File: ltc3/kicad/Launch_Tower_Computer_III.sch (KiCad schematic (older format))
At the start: 0 parts

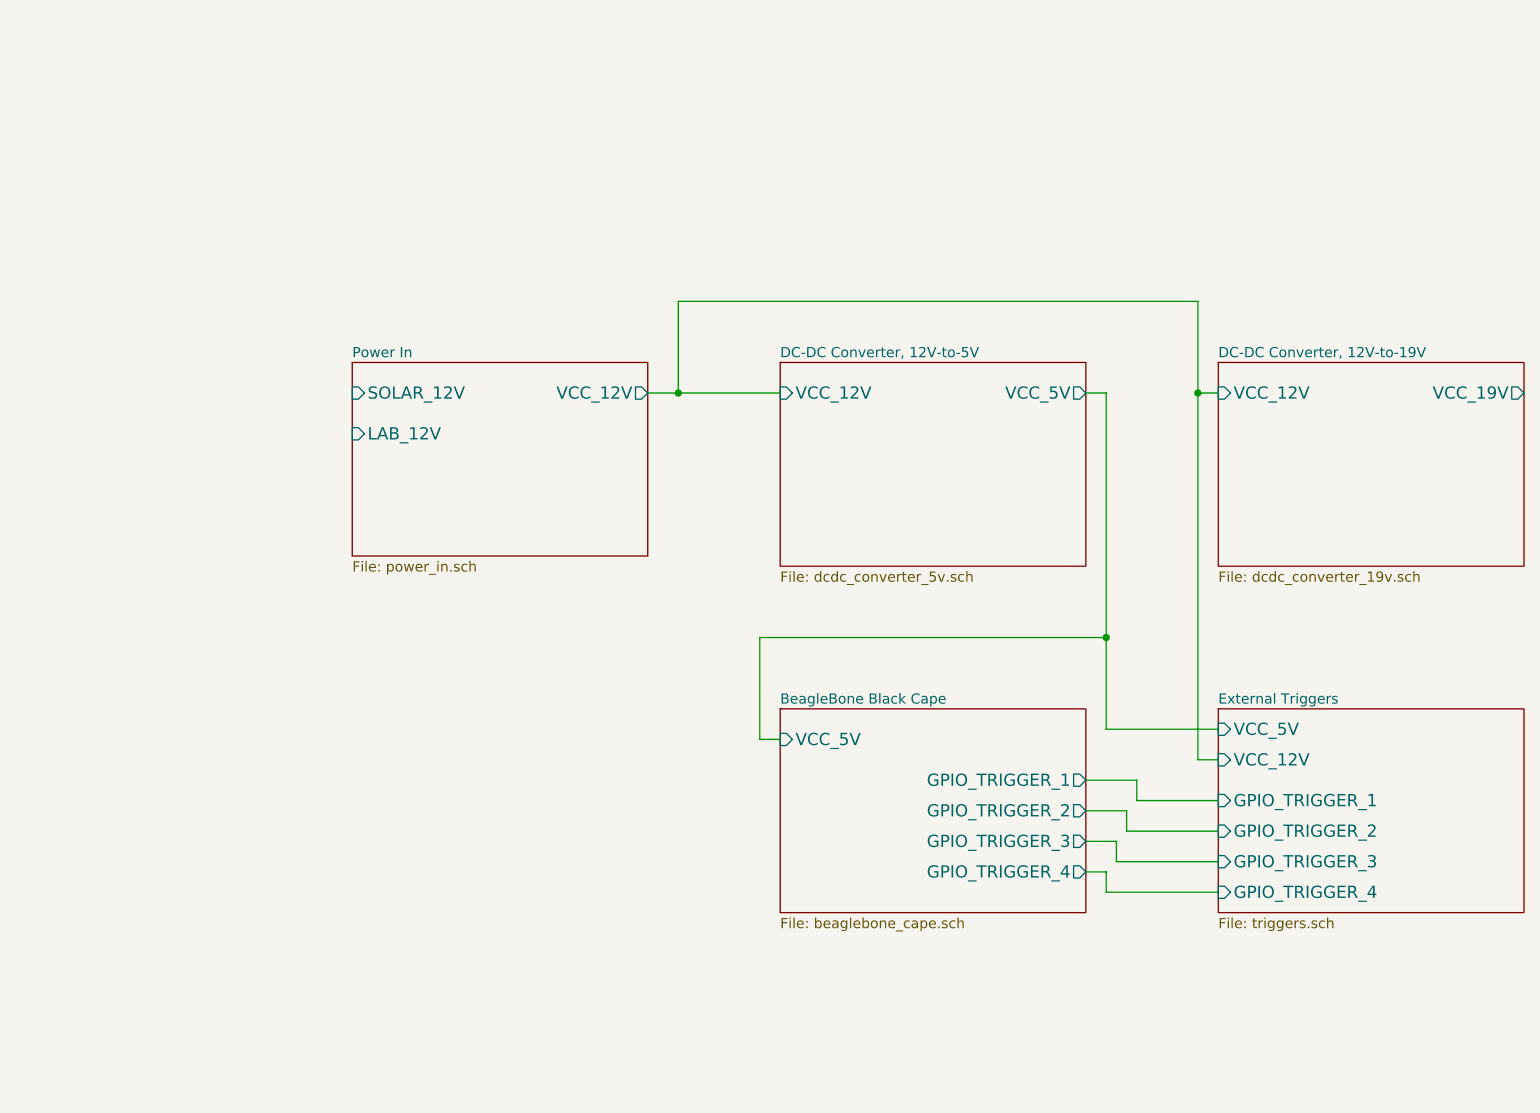
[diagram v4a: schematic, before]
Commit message: Incremental progress on LTC3 design spec, schematic.
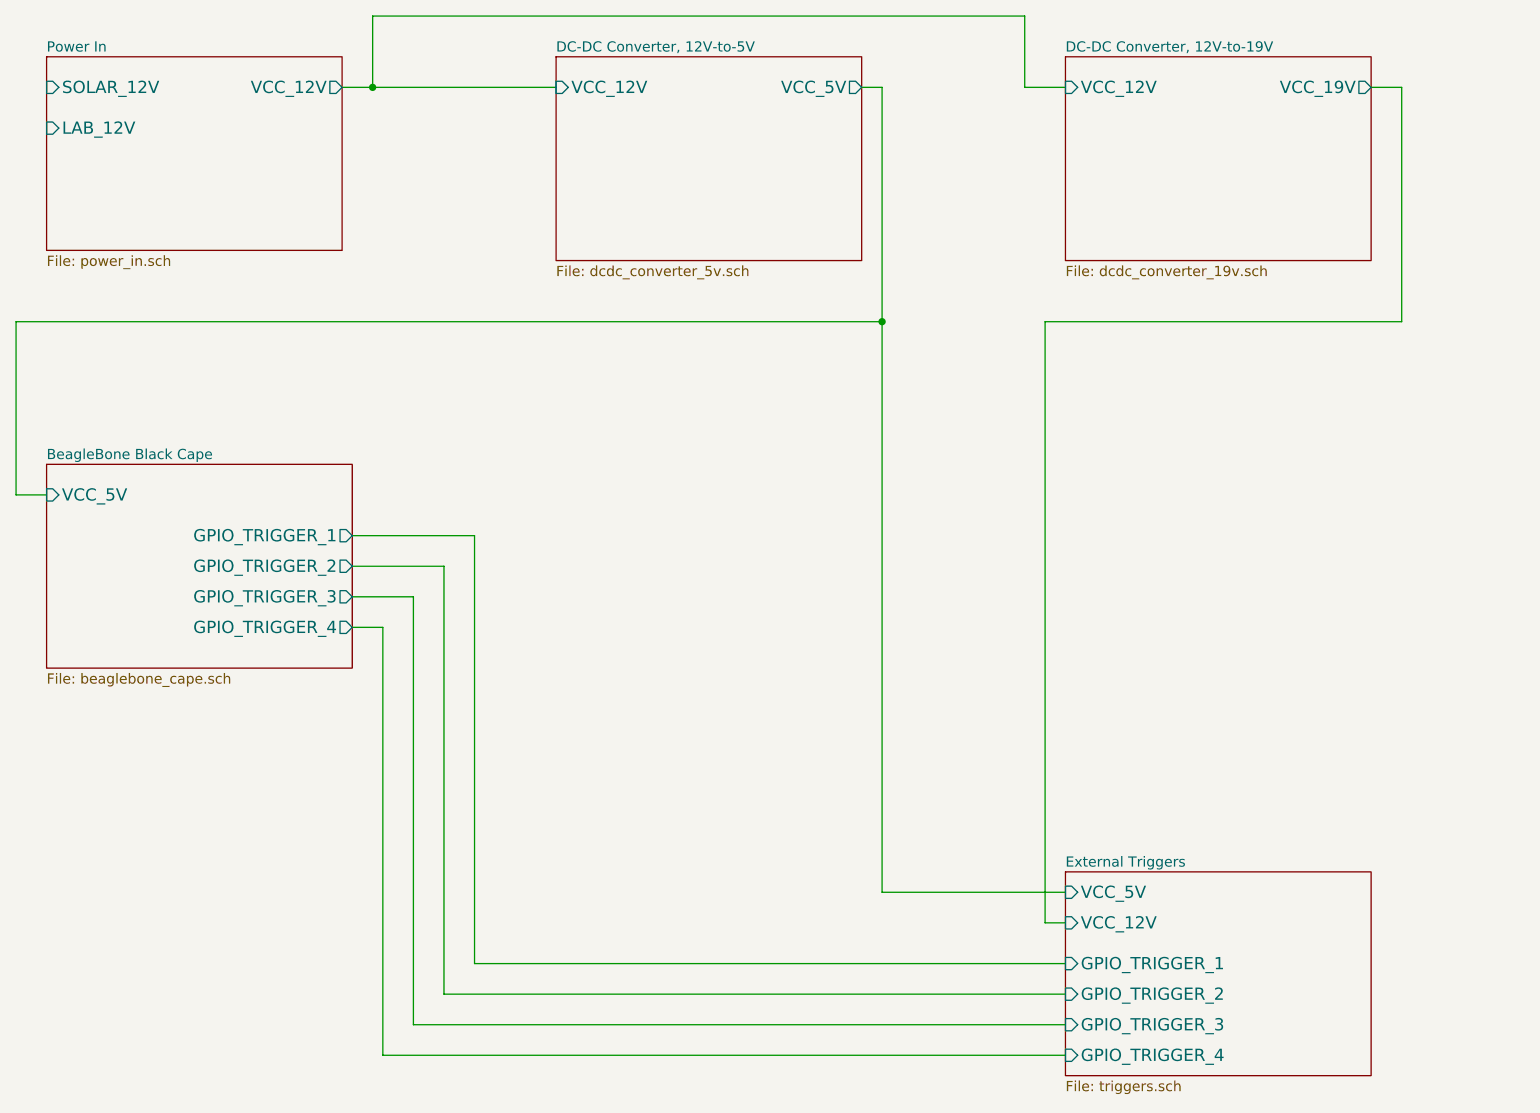
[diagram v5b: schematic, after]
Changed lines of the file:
@@
 Sheet 1 6
 Title "Launch Tower Computer III (LTC3)"
-Date "3 apr 2015"
+Date "4 apr 2015"
 Rev "1"
 Comp "Portland State Aerospace Society <http://psas.pdx.edu/>"
@@
 $EndDescr
 $Sheet
-S 2500 2600 1450 950
+S 1000 1100 1450 950
 U 551C8EE6
 F0 "Power In" 50
 F1 "power_in.sch" 50
-F2 "VCC_12V" O R 3950 2750 60
-F3 "SOLAR_12V" I L 2500 2750 60
-F4 "LAB_12V" I L 2500 2950 60
+F2 "VCC_12V" O R 2450 1250 60
+F3 "SOLAR_12V" I L 1000 1250 60
+F4 "LAB_12V" I L 1000 1450 60
 $EndSheet
 $Sheet
-S 4600 2600 1500 1000
+S 3500 1100 1500 1000
 U 550535FB
 F0 "DC-DC Converter, 12V-to-5V" 50
 F1 "dcdc_converter_5v.sch" 50
-F2 "VCC_5V" O R 6100 2750 60
-F3 "VCC_12V" I L 4600 2750 60
+F2 "VCC_5V" O R 5000 1250 60
+F3 "VCC_12V" I L 3500 1250 60
 $EndSheet
 $Sheet
-S 6750 2600 1500 1000
+S 6000 1100 1500 1000
 U 55053600
 F0 "DC-DC Converter, 12V-to-19V" 50
 F1 "dcdc_converter_19v.sch" 50
-F2 "VCC_19V" O R 8250 2750 60
-F3 "VCC_12V" I L 6750 2750 60
+F2 "VCC_19V" O R 7500 1250 60
+F3 "VCC_12V" I L 6000 1250 60
 $EndSheet
 $Sheet
-S 4600 4300 1500 1000
+S 1000 3100 1500 1000
 U 55051BA8
 F0 "BeagleBone Black Cape" 50
 F1 "beaglebone_cape.sch" 50
-F2 "VCC_5V" I L 4600 4450 60
-F3 "GPIO_TRIGGER_1" O R 6100 4650 60
-F4 "GPIO_TRIGGER_2" O R 6100 4800 60
-F5 "GPIO_TRIGGER_3" O R 6100 4950 60
-F6 "GPIO_TRIGGER_4" O R 6100 5100 60
+F2 "VCC_5V" I L 1000 3250 60
+F3 "GPIO_TRIGGER_1" O R 2500 3450 60
+F4 "GPIO_TRIGGER_2" O R 2500 3600 60
+F5 "GPIO_TRIGGER_3" O R 2500 3750 60
+F6 "GPIO_TRIGGER_4" O R 2500 3900 60
 $EndSheet
-Wire Wire Line
-	6100 2750 6200 2750
-Wire Wire Line
-	6200 2750 6200 4400
-Wire Wire Line
-	6200 3950 4500 3950
-Wire Wire Line
-	4500 3950 4500 4450
-Wire Wire Line
-	4500 4450 4600 4450
-Wire Wire Line
-	3950 2750 4600 2750
-Wire Wire Line
-	6650 2750 6750 2750
-Wire Wire Line
-	6200 4400 6750 4400
 $Sheet
-S 6750 4300 1500 1000
+S 6000 5100 1500 1000
 U 551C79BE
 F0 "External Triggers" 50
 F1 "triggers.sch" 50
-F2 "GPIO_TRIGGER_1" I L 6750 4750 60
-F3 "GPIO_TRIGGER_2" I L 6750 4900 60
-F4 "GPIO_TRIGGER_3" I L 6750 5050 60
-F5 "GPIO_TRIGGER_4" I L 6750 5200 60
-F6 "VCC_12V" I L 6750 4550 60
-F7 "VCC_5V" I L 6750 4400 60
+F2 "GPIO_TRIGGER_1" I L 6000 5550 60
+F3 "GPIO_TRIGGER_2" I L 6000 5700 60
+F4 "GPIO_TRIGGER_3" I L 6000 5850 60
+F5 "GPIO_TRIGGER_4" I L 6000 6000 60
+F6 "VCC_12V" I L 6000 5350 60
+F7 "VCC_5V" I L 6000 5200 60
 $EndSheet
 Wire Wire Line
-	6650 4550 6750 4550
-Connection ~ 6200 3950
+	2450 1250 3500 1250
 Wire Wire Line
-	4100 2750 4100 2300
+	2600 1250 2600 900
 Wire Wire Line
-	4100 2300 6650 2300
+	2600 900  5800 900
 Wire Wire Line
-	6650 2300 6650 4550
-Connection ~ 4100 2750
-Connection ~ 6650 2750
+	5800 900  5800 1250
 Wire Wire Line
-	6100 4650 6350 4650
+	5800 1250 6000 1250
+Connection ~ 2600 1250
 Wire Wire Line
-	6350 4650 6350 4750
+	5000 1250 5100 1250
 Wire Wire Line
-	6350 4750 6750 4750
+	5100 1250 5100 5200
 Wire Wire Line
-	6100 4800 6300 4800
+	5100 2400 850  2400
 Wire Wire Line
-	6300 4800 6300 4900
+	850  2400 850  3250
 Wire Wire Line
-	6300 4900 6750 4900
+	850  3250 1000 3250
 Wire Wire Line
-	6100 4950 6250 4950
+	5100 5200 6000 5200
+Connection ~ 5100 2400
 Wire Wire Line
-	6250 4950 6250 5050
+	6000 5350 5900 5350
 Wire Wire Line
-	6250 5050 6750 5050
+	5900 5350 5900 2400
 Wire Wire Line
-	6100 5100 6200 5100
+	5900 2400 7650 2400
 Wire Wire Line
-	6200 5100 6200 5200
+	7650 2400 7650 1250
 Wire Wire Line
-	6200 5200 6750 5200
+	7650 1250 7500 1250
+Wire Wire Line
+	2500 3900 2650 3900
+Wire Wire Line
+	2650 3900 2650 6000
+Wire Wire Line
+	2650 6000 6000 6000
+Wire Wire Line
+	2500 3750 2800 3750
+Wire Wire Line
+	2800 3750 2800 5850
+Wire Wire Line
+	2800 5850 6000 5850
+Wire Wire Line
+	2500 3600 2950 3600
+Wire Wire Line
+	2950 3600 2950 5700
+Wire Wire Line
+	2950 5700 6000 5700
+Wire Wire Line
+	2500 3450 3100 3450
+Wire Wire Line
+	3100 3450 3100 5550
+Wire Wire Line
+	3100 5550 6000 5550
 $EndSCHEMATC
